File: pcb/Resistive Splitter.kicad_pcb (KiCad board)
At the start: 2 copper layers, 75 x 40 mm, 6 parts, among them J1 SMA 50, J2 SMA 50, J3 SMA 50

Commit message: semmantic error
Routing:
- net Net-(R1-Pad2): track 42.6 -> 41.8 mm
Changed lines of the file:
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@@
 		)
+	)
+	(segment
+		(start 69.905 10)
+		(end 52.9625 10)
+		(width 0.62)
+		(layer "F.Cu")
+		(net "Net-(J2-In)")
 	)
 	(via
@@
 		(filling no)
 		(net "GND")
+	)
+	(segment
+		(start 35.15 20.05)
+		(end 45.1 30)
+		(width 0.62)
+		(layer "F.Cu")
+		(net "Net-(R1-Pad2)")
+	)
+	(segment
+		(start 47 30)
+		(end 45.9 30)
+		(width 0.62)
+		(layer "F.Cu")
+		(net "Net-(R1-Pad2)")
+	)
+	(segment
+		(start 47 10)
+		(end 45.2 10)
+		(width 0.62)
+		(layer "F.Cu")
+		(net "Net-(R1-Pad2)")
+	)
+	(segment
+		(start 45.1 30)
+		(end 45.9 30)
+		(width 0.62)
+		(layer "F.Cu")
+		(net "Net-(R1-Pad2)")
+	)
+	(segment
+		(start 26.0625 20.05)
+		(end 26.0125 20)
+		(width 0.62)
+		(layer "F.Cu")
+		(net "Net-(R1-Pad2)")
+	)
+	(segment
+		(start 45.2 10)
+		(end 35.15 20.05)
+		(width 0.62)
+		(layer "F.Cu")
+		(net "Net-(R1-Pad2)")
+	)
+	(segment
+		(start 35.1 20)
+		(end 26.0625 20)
+		(width 0.62)
+		(layer "F.Cu")
+		(net "Net-(R1-Pad2)")
+	)
+	(segment
+		(start 35.635 20.535)
+		(end 35.1 20)
+		(width 0.62)
+		(layer "F.Cu")
+		(net "Net-(R1-Pad2)")
+	)
+	(segment
+		(start 70.905 30)
+		(end 52.9625 30)
+		(width 0.62)
+		(layer "F.Cu")
+		(net "Net-(J3-In)")
 	)
 	(segment
@@
 		(net "Net-(J1-In)")
 	)
-	(segment
-		(start 69.905 10)
-		(end 52.9625 10)
-		(width 0.62)
-		(layer "F.Cu")
-		(net "Net-(J2-In)")
-	)
-	(segment
-		(start 70.905 30)
-		(end 52.9625 30)
-		(width 0.62)
-		(layer "F.Cu")
-		(net "Net-(J3-In)")
-	)
-	(segment
-		(start 35.15 20.05)
-		(end 45.1 30)
-		(width 0.62)
-		(layer "F.Cu")
-		(net "Net-(R1-Pad2)")
-	)
-	(segment
-		(start 47 30)
-		(end 45.9 30)
-		(width 0.62)
-		(layer "F.Cu")
-		(net "Net-(R1-Pad2)")
-	)
-	(segment
-		(start 47 10)
-		(end 45.2 10)
-		(width 0.62)
-		(layer "F.Cu")
-		(net "Net-(R1-Pad2)")
-	)
-	(segment
-		(start 45.1 30)
-		(end 45.9 30)
-		(width 0.62)
-		(layer "F.Cu")
-		(net "Net-(R1-Pad2)")
-	)
-	(segment
-		(start 26.0625 20.05)
-		(end 26.0125 20)
-		(width 0.62)
-		(layer "F.Cu")
-		(net "Net-(R1-Pad2)")
-	)
-	(segment
-		(start 31.35 20.05)
-		(end 26.0625 20.05)
-		(width 0.62)
-		(layer "F.Cu")
-		(net "Net-(R1-Pad2)")
-	)
-	(segment
-		(start 45.2 10)
-		(end 35.15 20.05)
-		(width 0.62)
-		(layer "F.Cu")
-		(net "Net-(R1-Pad2)")
-	)
-	(segment
-		(start 31.35 20.05)
-		(end 32.8 20.05)
-		(width 0.62)
-		(layer "F.Cu")
-		(net "Net-(R1-Pad2)")
-	)
-	(segment
-		(start 35.15 20.05)
-		(end 31.35 20.05)
-		(width 0.62)
-		(layer "F.Cu")
-		(net "Net-(R1-Pad2)")
-	)
 	(zone

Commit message: pcb update
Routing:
- net Net-(R1-Pad2): track 41.8 -> 41.2 mm
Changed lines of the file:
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@@
 	)
 	(segment
-		(start 35.15 20.05)
-		(end 45.1 30)
+		(start 35.2 20)
+		(end 35.1 20)
 		(width 0.62)
 		(layer "F.Cu")
@@
 	)
 	(segment
-		(start 47 30)
-		(end 45.9 30)
-		(width 0.62)
-		(layer "F.Cu")
-		(net "Net-(R1-Pad2)")
-	)
-	(segment
-		(start 47 10)
-		(end 45.2 10)
-		(width 0.62)
-		(layer "F.Cu")
-		(net "Net-(R1-Pad2)")
-	)
-	(segment
-		(start 45.1 30)
-		(end 45.9 30)
+		(start 35.1 20)
+		(end 45.1 30)
 		(width 0.62)
 		(layer "F.Cu")
@@
 	)
 	(segment
-		(start 45.2 10)
-		(end 35.15 20.05)
-		(width 0.62)
-		(layer "F.Cu")
-		(net "Net-(R1-Pad2)")
-	)
-	(segment
 		(start 35.1 20)
 		(end 26.0625 20)
@@
 	)
 	(segment
-		(start 35.635 20.535)
-		(end 35.1 20)
+		(start 45.2 10)
+		(end 35.2 20)
 		(width 0.62)
 		(layer "F.Cu")
+		(net "Net-(R1-Pad2)")
+	)
+	(segment
+		(start 45.1 30)
+		(end 47 30)
+		(width 0.62)
+		(layer "F.Cu")
+		(net "Net-(R1-Pad2)")
+	)
+	(segment
+		(start 47 10)
+		(end 45.2 10)
+		(width 0.62)
+		(layer "F.Cu")

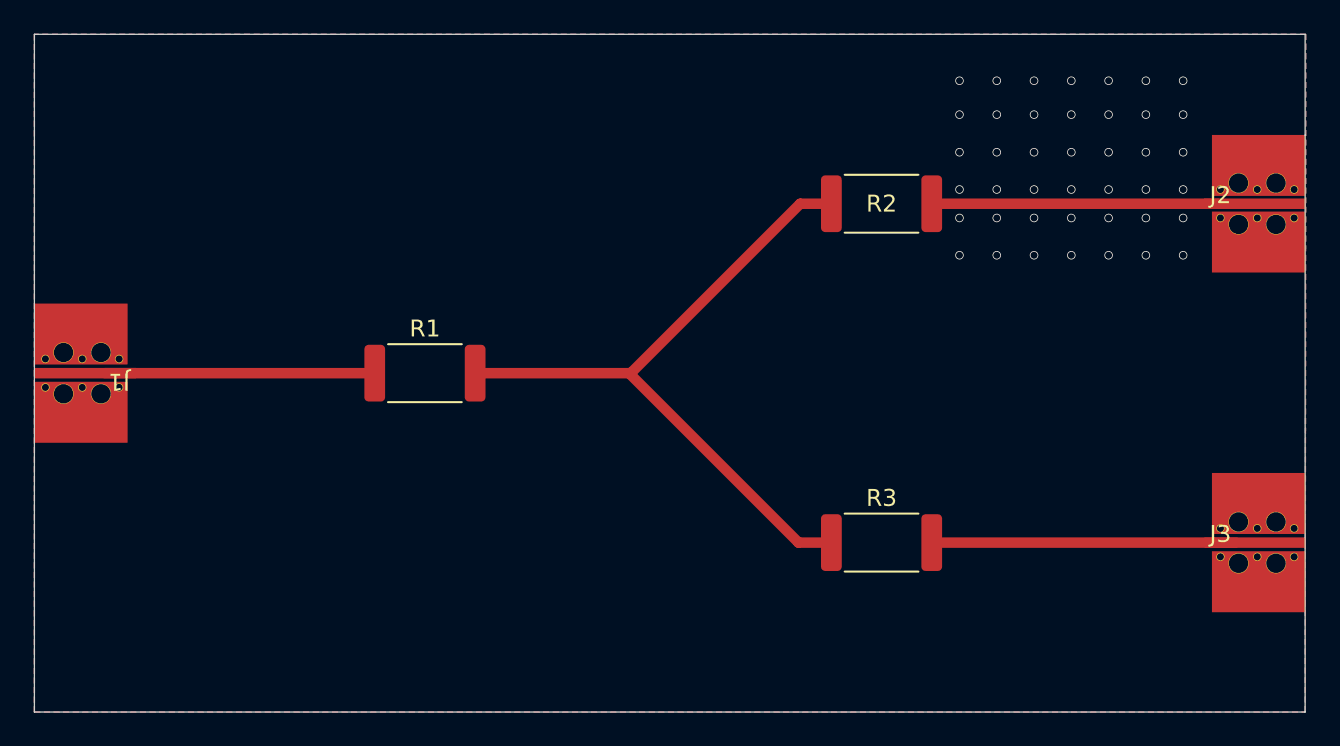
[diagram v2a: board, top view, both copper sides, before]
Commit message: add vias
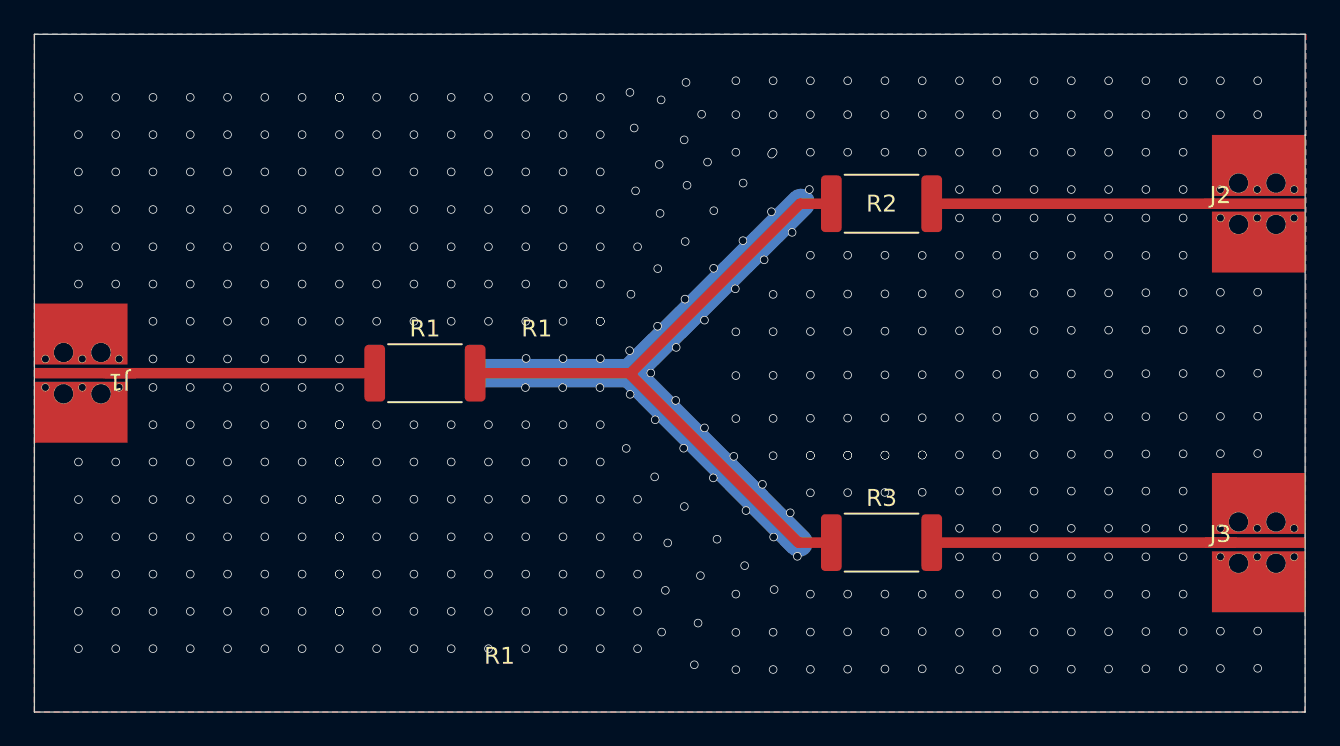
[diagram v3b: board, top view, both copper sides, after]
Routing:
- net GND: vias 42 -> 504
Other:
- board text added: "J1"
- board text added: "J2"
- board text added: "R1"
